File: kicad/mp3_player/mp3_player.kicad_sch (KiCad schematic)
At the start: 26 parts, among them J1 microSD, SW1 Boot, SW2 Reset, SW3 RotaryEncoder_Switch, U1 MPU6500-breakout, U2 HC-SR04_Ultrasonic_Sensor, U3 ESP32-S3-WROOM-1, U4 AHT20_BMP280

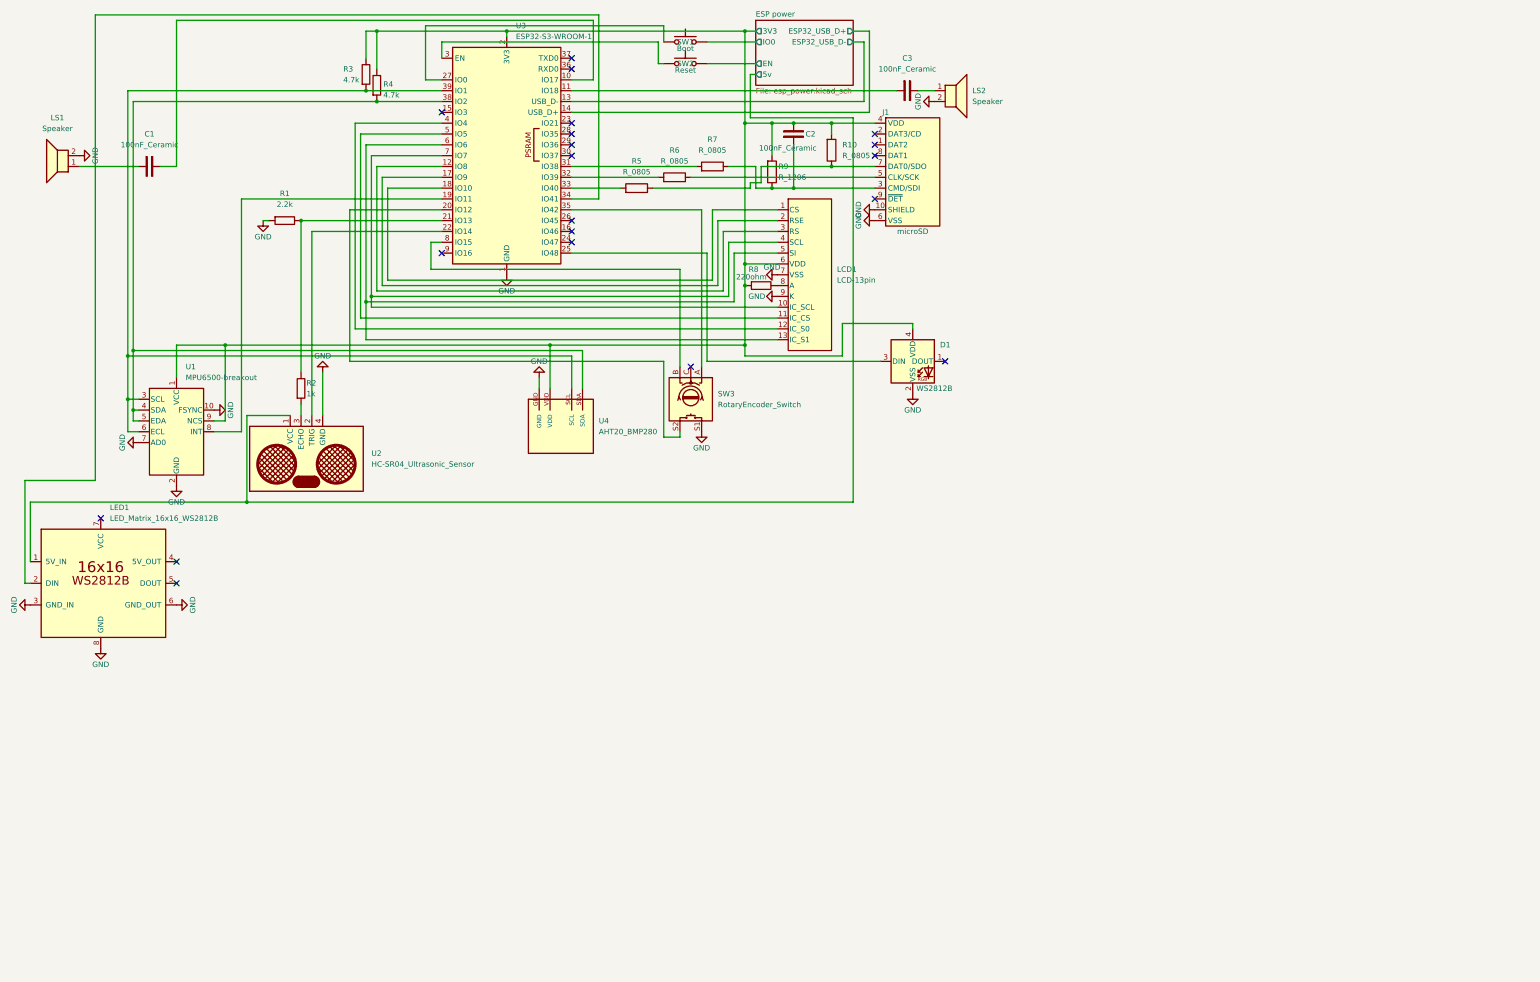
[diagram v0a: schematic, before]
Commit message: [UPDATE] the desing of the schematic to use the current audio module
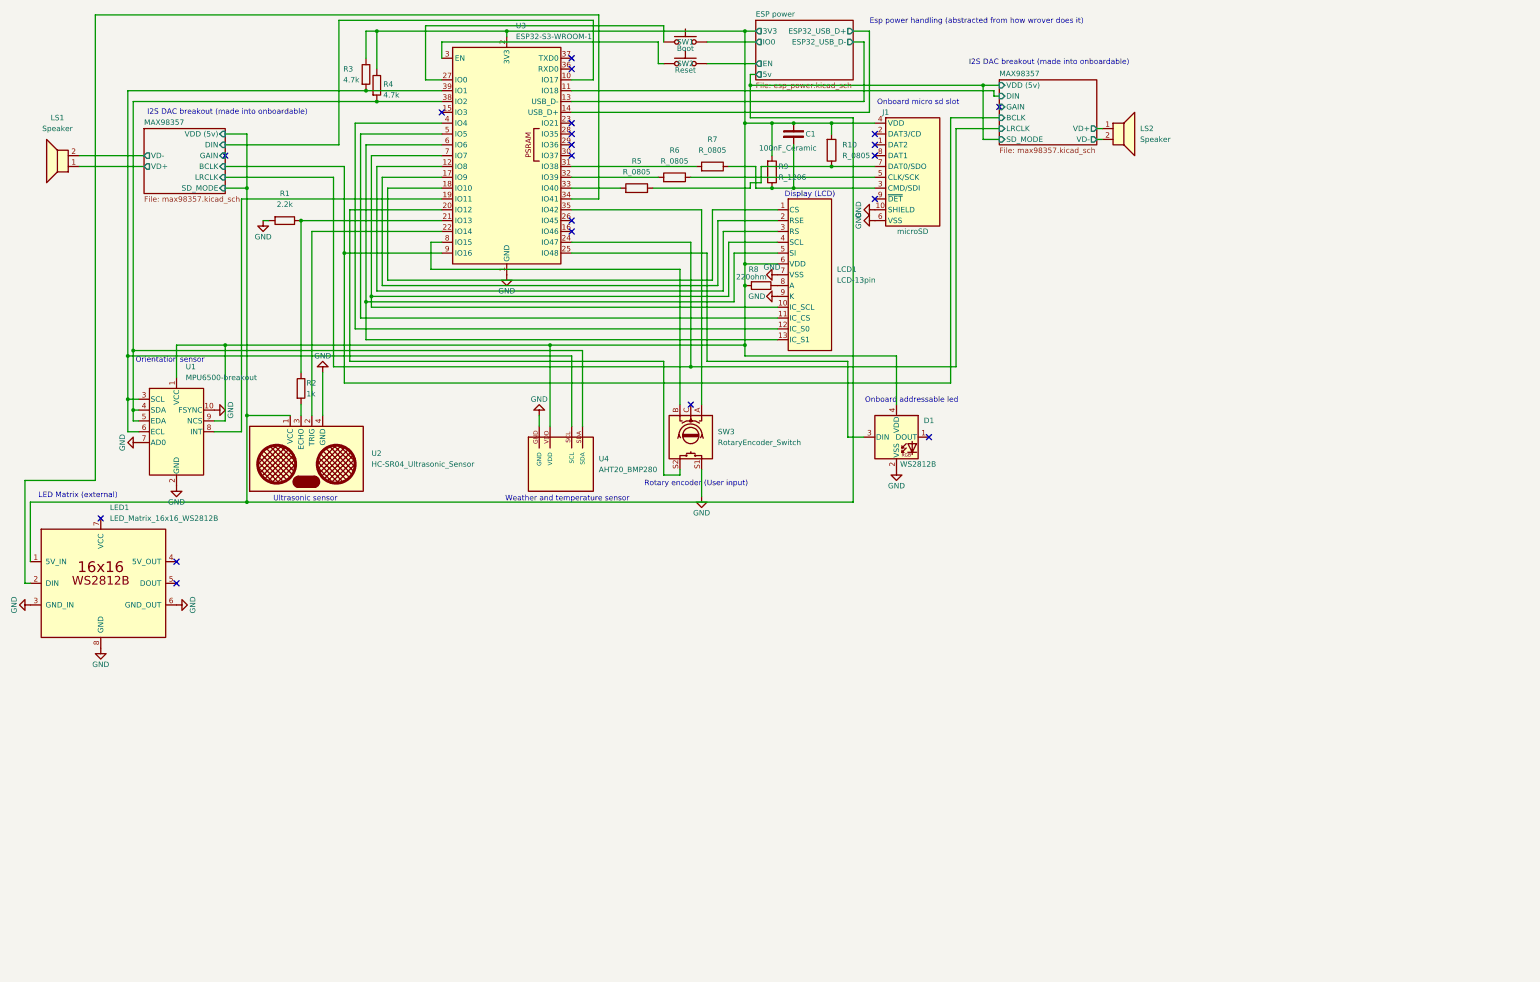
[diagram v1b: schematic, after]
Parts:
- removed C1, C3: 100nF_Ceramic, Capacitor_THT:C_Disc_D5.0mm_W2.5mm_P2.50mm, symbol PCM_SL_Capacitors:100nF_Ceramic
- renumbered C2 to C1
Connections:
- net GND: no longer LS1.2, LS2.2
- net MAX98357/VD+: now reaches LS1.1
- net MAX98357/DIN: now reaches U3.10 (IO17)
- net MAX98357/DIN: now reaches U3.11 (IO18)
- net MAX98357/LRCLK: now reaches U3.24 (IO47)
- net MAX98357/BCLK: now reaches U3.9 (IO16)
- net MAX98357/VD+: now reaches LS2.1
- new net MAX98357/VD-: LS2.2
- new net MAX98357/VD-: LS1.2
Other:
- added sheet MAX98357 (max98357.kicad_sch)
- note added: "Display (LCD)"
- note added: "Esp power handling (abstracted from how wrover does it)"
- note added: "I2S DAC breakout (made into onboardable)"
- note added: "LED Matrix (external)"
- note added: "Onboard addressable led"
- note added: "Onboard micro sd slot"
- note added: "Orientation sensor"
- note added: "Rotary encoder (User input)"
- note added: "Ultrasonic sensor"
- note added: "Weather and temperature sensor"
- moved on the sheet: D1, LS2, SW3, U4

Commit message: [UPDATE] the scheamtic to fix the issue with the pot not detecting volume
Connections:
- net MAX98357/DIN is gone; now on net MAX98357/DIN: U3.11 (IO18)
- net MAX98357/VD+ is gone; now on net MAX98357/VD+: LS1.1
- net MAX98357/VD- is gone; now on net MAX98357/VD-: LS1.2
- net GND: now also SW3.C
- net MAX98357/DIN: no longer U3.10 (IO17)
- net MAX98357/VD+: no longer LS2.1
- net MAX98357/VD-: no longer LS2.2
- new net MAX98357/DIN: U3.10 (IO17)
- new net MAX98357/VD+: LS2.1
- new net MAX98357/VD-: LS2.2
- no-connect marks 20 -> 19
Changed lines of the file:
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@@
 	)
 	(no_connect
-		(at 176.53 104.14)
-	)
-	(no_connect
 		(at 248.92 34.29)
 	)
@@
 	(wire
 		(pts
+			(xy 176.53 101.6) (xy 176.53 104.14)
+		)
+		(stroke
+			(width 0)
+			(type default)
+		)
+	)
+	(wire
+		(pts
 			(xy 101.6 78.74) (xy 185.42 78.74)
 		)
@@
 					(unit 1)
 				)
+			)
+		)
+	)
+	(symbol
+		(lib_id "PCM_SparkFun-PowerSymbol:GND")
+		(at 176.53 101.6 180)
+		(unit 1)
+		(body_style 1)
+		(exclude_from_sim no)
+		(in_bom yes)
+		(on_board yes)
+		(in_pos_files yes)
+		(dnp no)
+		(fields_autoplaced yes)
+		(property "Reference" "#PWR036"
+			(at 176.53 95.25 0)
+			(hide yes)
+			(show_name no)
+			(do_not_autoplace no)
+			(effects
+				(font
+					(size 1.27 1.27)
+				)
+			)
+		)
+		(property "Value" "GND"
+			(at 176.53 97.79 0)
+			(show_name no)
+			(do_not_autoplace yes)
+			(effects
+				(font
+					(size 1.27 1.27)
+				)
+			)
+		)
+		(property "Footprint" ""
+			(at 176.53 101.6 0)
+			(hide yes)
+			(show_name no)
+			(do_not_autoplace no)
+			(effects
+				(font
+					(size 1.27 1.27)
+				)
+			)
+		)
+		(property "Datasheet" ""
+			(at 176.53 101.6 0)
+			(hide yes)
+			(show_name no)
+			(do_not_autoplace no)
+			(effects
+				(font
+					(size 1.27 1.27)
+				)
+			)
+		)
+		(property "Description" "Power symbol creates a global label with name \"GND\" , ground"
+			(at 176.53 92.71 0)
+			(hide yes)
+			(show_name no)
+			(do_not_autoplace no)
+			(effects
+				(font
+					(size 1.27 1.27)
+				)
+			)
+		)
+		(pin "1"
+		)
+		(instances
+			(project "mp3_player"
+				(path "/0f0043d3-9467-400d-886a-57a73f910f34"
+					(reference "#PWR036")
+					(unit 1)
+				)

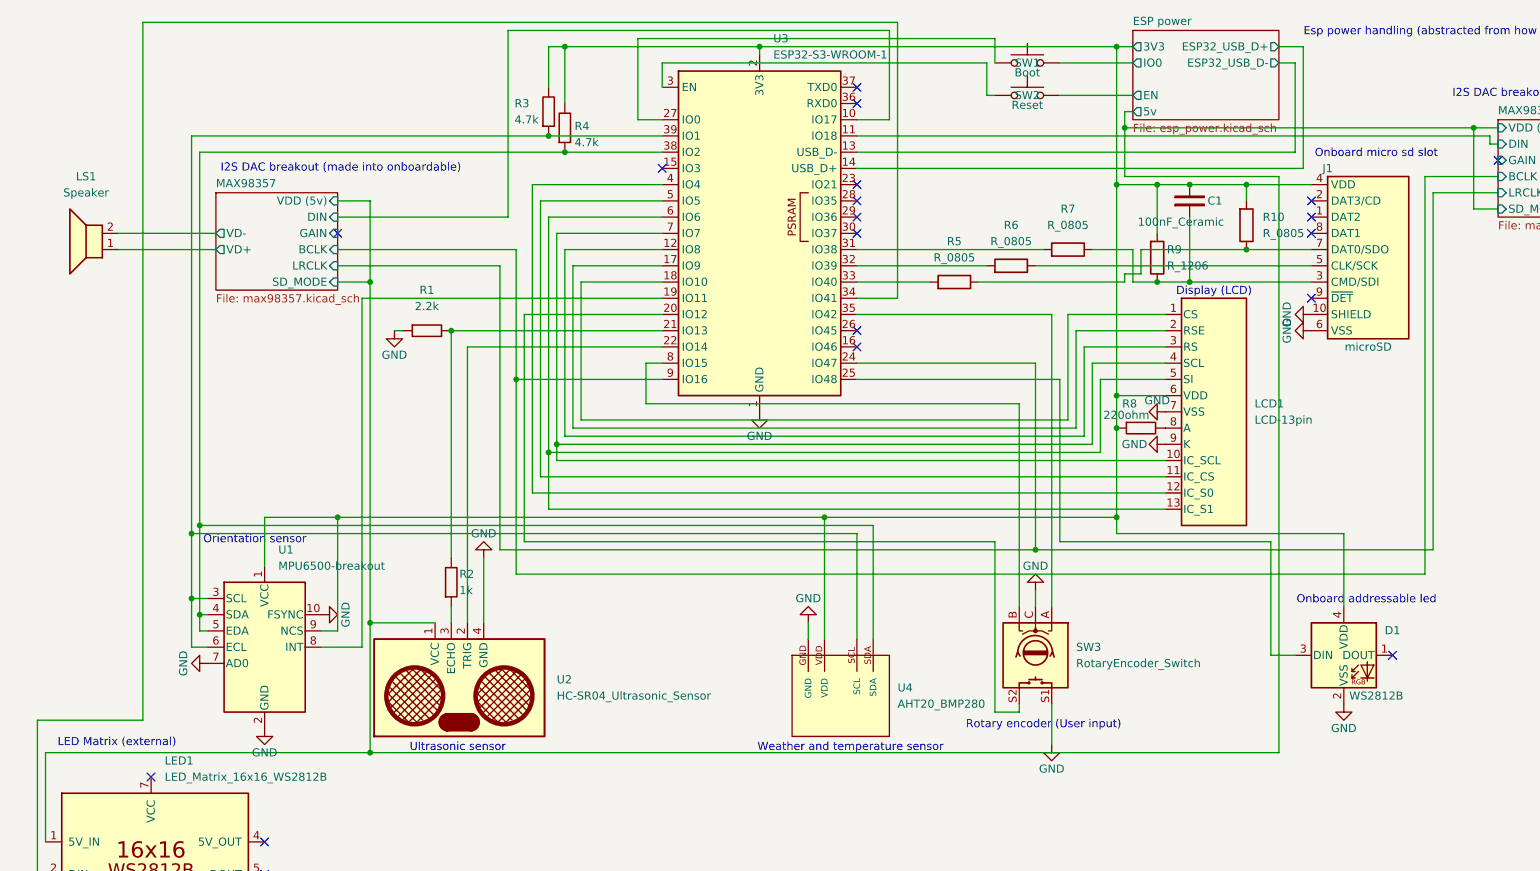
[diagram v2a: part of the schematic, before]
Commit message: [FIX] the schematic tracking issue in KiCad
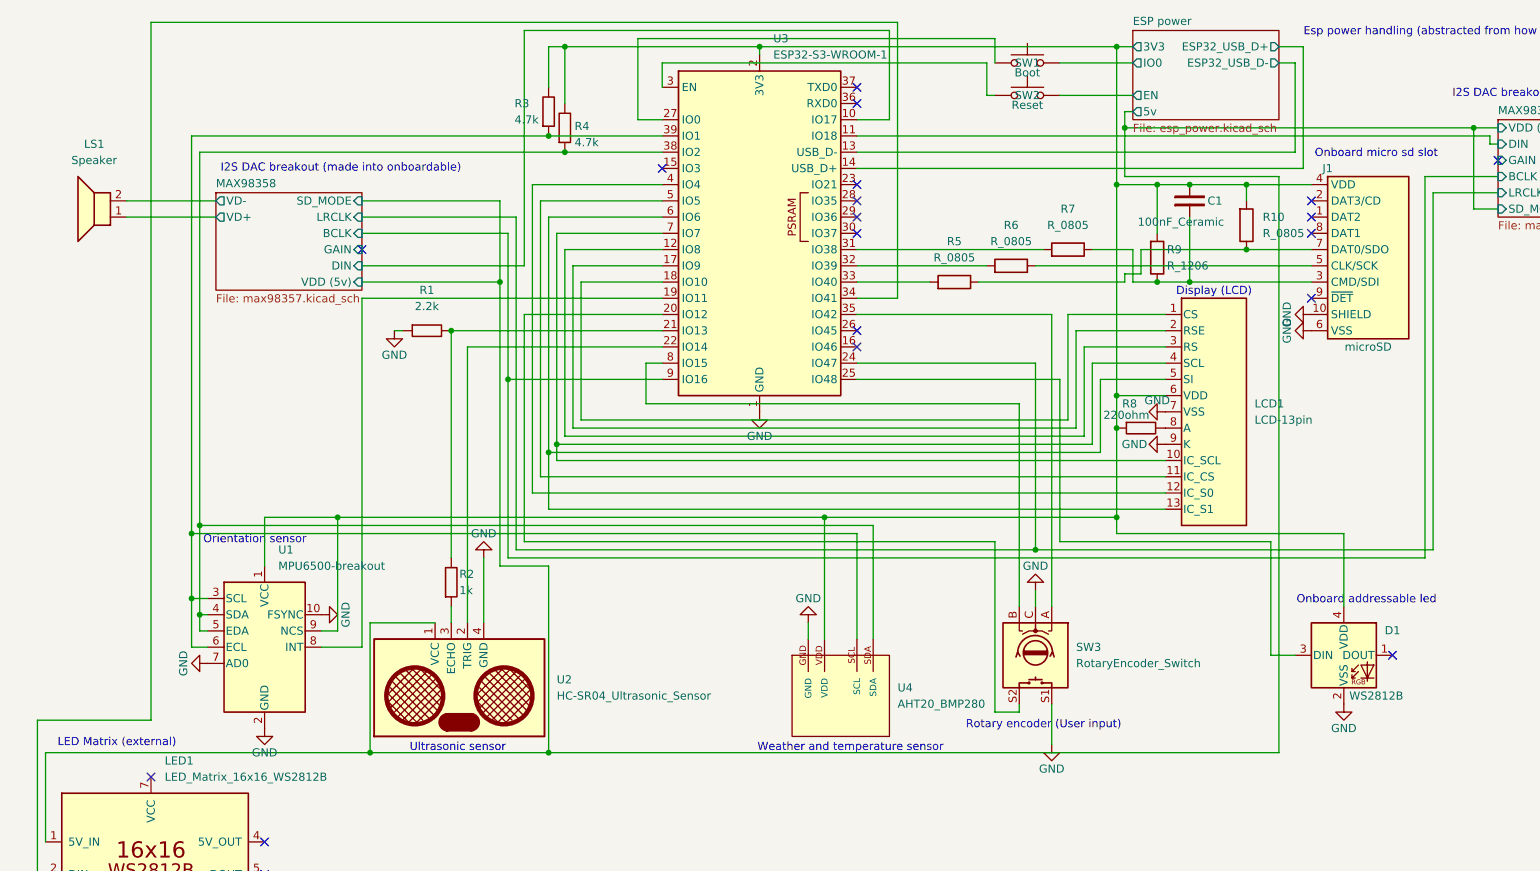
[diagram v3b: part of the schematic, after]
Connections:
- net MAX98357/DIN is gone; now on net MAX98357/DIN: U3.11 (IO18)
- net MAX98357/DIN: no longer U3.10 (IO17)
- net MAX98357/VD+ renamed MAX98358/VD+
- net MAX98357/VD- renamed MAX98358/VD-
- new net MAX98358/DIN: U3.10 (IO17)
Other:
- added sheet MAX98358 (max98357.kicad_sch)
- moved on the sheet: LS1
